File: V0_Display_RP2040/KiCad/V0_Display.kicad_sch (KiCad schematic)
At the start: 46 parts, among them J2 I2C Header 1, J3 SWD, J4 USB-TYPE-C-018, J7 USB_Header, J8 Conn_01x02, SW1 RESET, SW5 BOOTSEL, SW6 Killswitch, SW7 Rotary_Encoder_Switch, U1 AP2127K-3.3, U2 USBLC6-2P6, U3 74LVC1G17, U4 W25Q16JVUXIQ_TR, U5 RP2040, Y1 12Mhz

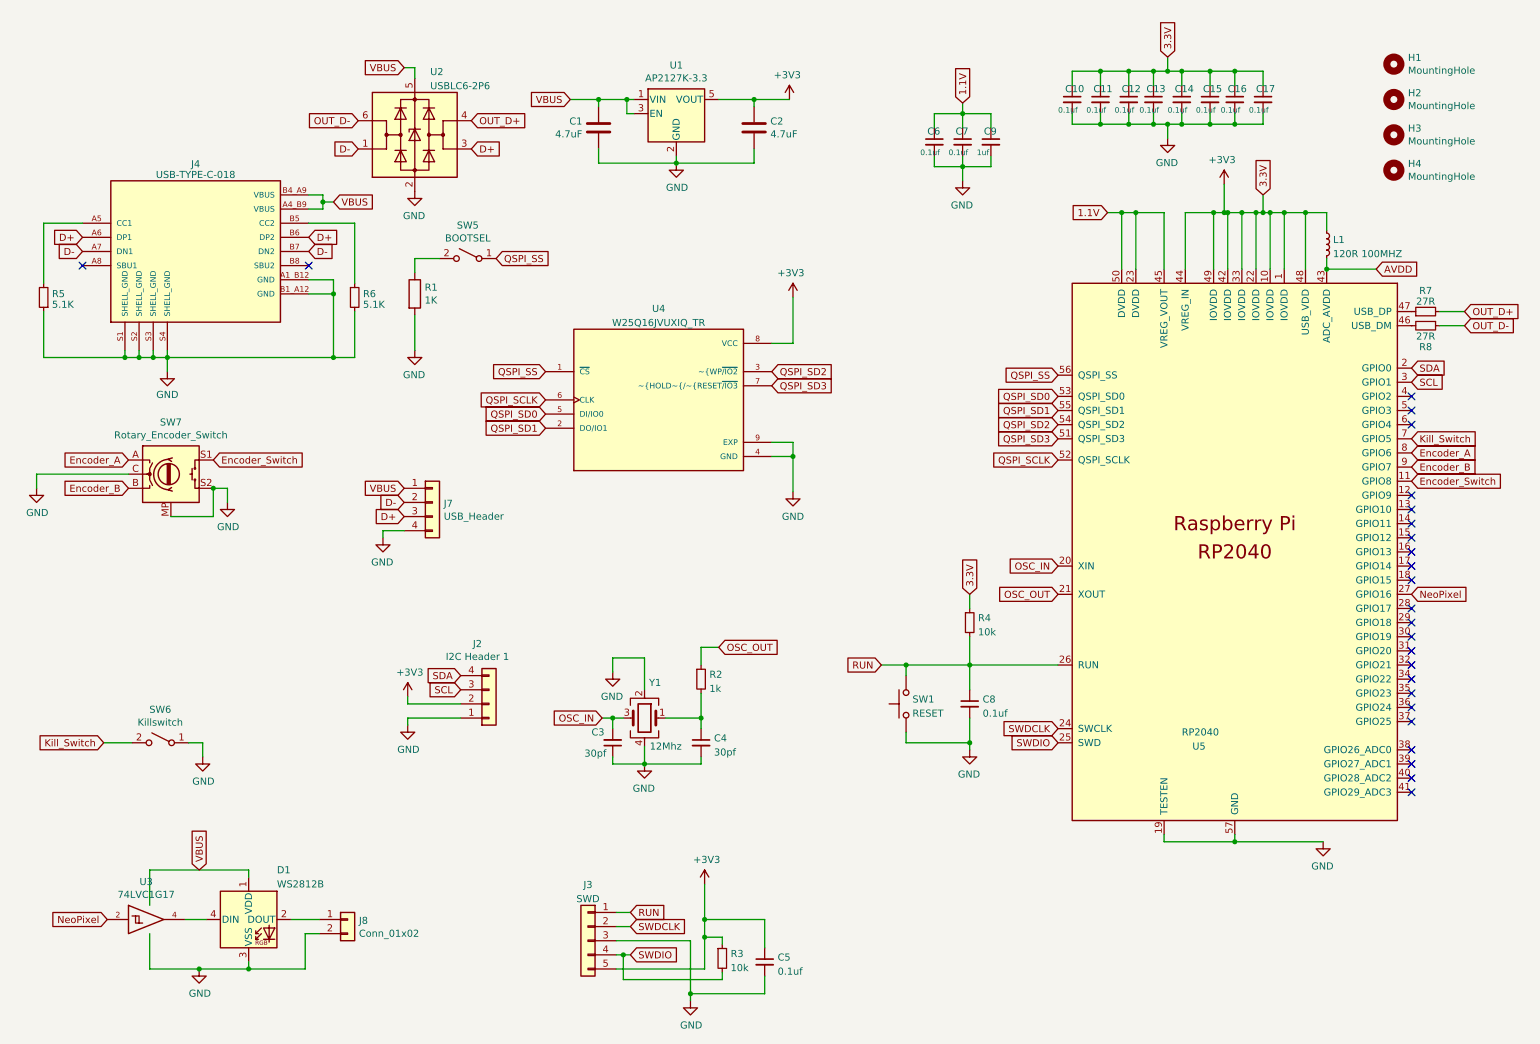
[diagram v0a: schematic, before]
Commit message: Several updates
Update to 2 layer board
vertical USB connector
updated fonts
Regenerated gerbers, BOM, and placement file
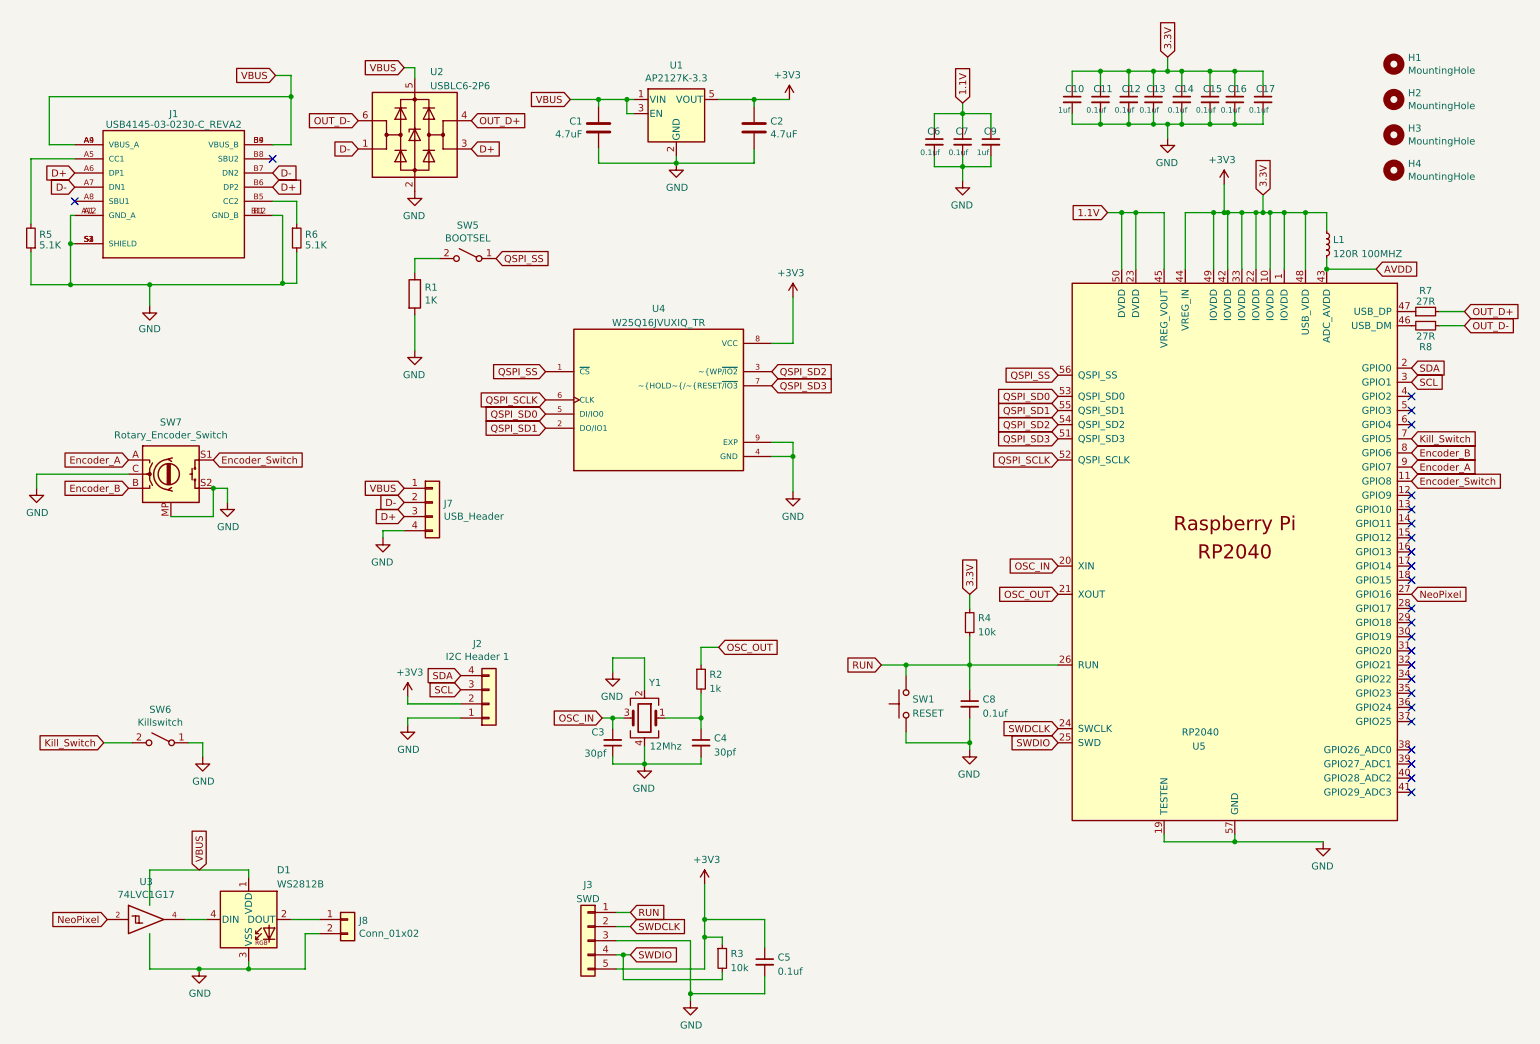
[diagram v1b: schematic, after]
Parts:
- removed J4: USB-TYPE-C-018, Voron0 2040 display:GCT_USB4105-GF-A, symbol Voron0 2040 library:USB4105-GF-A
- added J1: USB4145-03-0230-C_REVA2, USB4145-03-0230-C_REVA2:GCT_USB4145-03-0230-C_REVA2, symbol USB4145-03-0230-C_REVA2:USB4145-03-0230-C_REVA2
- C1, C2: symbol Voron0 2040 library:C -> Voron0 2040 display:C
- C10: value 0.1uf -> 1uf; symbol Voron0 2040 library:C_Small -> Voron0 2040 display:C_Small; LCSC C129131 -> C106254
- C11, C12, C13, C14, C15, C16, C17, C3, C4, C5, C6, C7, C8, C9: symbol Voron0 2040 library:C_Small -> Voron0 2040 display:C_Small
- D1: symbol Voron0 2040 library:WS2812B -> Voron0 2040 display:WS2812B
- H1, H2, H3, H4: symbol Voron0 2040 library:MountingHole -> Voron0 2040 display:MountingHole
- J2, J7: symbol Voron0 2040 library:Conn_01x04 -> Voron0 2040 display:Conn_01x04
- J3: symbol Voron0 2040 library:Conn_01x05 -> Voron0 2040 display:Conn_01x05
- J8: symbol Voron0 2040 library:Conn_01x02 -> Voron0 2040 display:Conn_01x02
- L1: symbol Voron0 2040 library:L_Small -> Voron0 2040 display:L_Small
- R1: symbol Voron0 2040 library:R -> Voron0 2040 display:R
- R2, R3, R4, R5, R6: symbol Voron0 2040 library:R_Small -> Voron0 2040 display:R_Small
- R7, R8: symbol Voron0 2040 library:R_Small -> Device:R_Small
- SW1: symbol Voron0 2040 library:SW_Push -> Voron0 2040 display:SW_Push
- SW5, SW6: symbol Voron0 2040 library:SW_SPST -> Voron0 2040 display:SW_SPST
- SW7: symbol Voron0 2040 library:Rotary_Encoder_Switch -> Voron0 2040 display:Rotary_Encoder_Switch
- U1: symbol Voron0 2040 library:AP2127K-3.3 -> Voron0 2040 display:AP2127K-3.3
- U2: symbol Voron0 2040 library:USBLC6-2P6 -> Voron0 2040 display:USBLC6-2P6
- U3: symbol Voron0 2040 library:74LVC1G17 -> Voron0 2040 display:74LVC1G17
- U4: symbol Voron0 2040 library:W25Q16JVUXIQ_TR -> Voron0 2040 display:W25Q16JVUXIQ_TR
- U5: symbol Voron0 2040 library:RP2040 -> Voron0 2040 display:RP2040
- Y1: symbol Voron0 2040 library:Crystal_GND24 -> Voron0 2040 display:Crystal_GND24
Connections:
- net D+: now also J1.A6 (DP1), J1.B6 (DP2)
- net D-: now also J1.A7 (DN1), J1.B7 (DN2)
- net Encoder_A: now also U5.9 (GPIO7); no longer U5.8 (GPIO6)
- net Encoder_B: now also U5.8 (GPIO6); no longer U5.9 (GPIO7)
- net GND: now also J1.A1 (GND_A), J1.A12 (GND_A), J1.B1 (GND_B), J1.B12 (GND_B), J1.S1 (SHIELD), J1.S2 (SHIELD), J1.S3 (SHIELD), J1.S4 (SHIELD)
- net VCC: now also J1.A4 (VBUS_A), J1.A9 (VBUS_A), J1.B4 (VBUS_B), J1.B9 (VBUS_B)
- net at R5.2: now also J1.A5 (CC1)
- net at R6.1: now also J1.B5 (CC2)
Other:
- moved on the sheet: R5, R6

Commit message: Update #2
Changed to SMD push buttons
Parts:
- SW1, SW5, SW6: footprint Voron0 2040 display:SW_PUSH_6mm -> Library:SW_Push_1P1T_NO_4.5x4.5mm; LCSC (none) -> C843607; MPN MJTP1230 -> (none); now in the parts list
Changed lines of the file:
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@@
   )
   (symbol (lib_id "Voron0 2040 display:SW_SPST") (at 95.25 55.245 0) (mirror y) (unit 1)
-    (in_bom no) (on_board yes) (dnp no)
+    (in_bom yes) (on_board yes) (dnp no)
     (property "Reference" "SW5" (at 95.25 49.276 0)
       (effects (font (size 1.27 1.27)))
@@
       (effects (font (size 1.27 1.27)))
     )
-    (property "Footprint" "Voron0 2040 display:SW_PUSH_6mm" (at 95.25 55.245 0)
+    (property "Footprint" "Library:SW_Push_1P1T_NO_4.5x4.5mm" (at 95.25 55.245 0)
       (effects (font (size 1.27 1.27)) hide)
     )
@@
       (effects (font (size 1.27 1.27)) hide)
     )
-    (property "MPN" "MJTP1230" (at 95.25 55.245 0)
+    (property "LCSC" "C843607" (at 95.25 55.245 0)
       (effects (font (size 1.27 1.27)) hide)
     )
@@
   )
   (symbol (lib_id "Voron0 2040 display:SW_SPST") (at 40.005 142.24 0) (mirror y) (unit 1)
-    (in_bom no) (on_board yes) (dnp no)
+    (in_bom yes) (on_board yes) (dnp no)
     (property "Reference" "SW6" (at 40.005 136.271 0)
       (effects (font (size 1.27 1.27)))
@@
       (effects (font (size 1.27 1.27)))
     )
-    (property "Footprint" "Voron0 2040 display:SW_PUSH_6mm" (at 40.005 142.24 0)
+    (property "Footprint" "Library:SW_Push_1P1T_NO_4.5x4.5mm" (at 40.005 142.24 0)
       (effects (font (size 1.27 1.27)) hide)
     )
@@
       (effects (font (size 1.27 1.27)) hide)
     )
-    (property "MPN" "MJTP1230" (at 40.005 142.24 0)
+    (property "LCSC" "C843607" (at 40.005 142.24 0)
       (effects (font (size 1.27 1.27)) hide)
     )
@@
   )
   (symbol (lib_id "Voron0 2040 display:SW_Push") (at 173.99 135.255 90) (unit 1)
-    (in_bom no) (on_board yes) (dnp no) (fields_autoplaced)
+    (in_bom yes) (on_board yes) (dnp no) (fields_autoplaced)
     (property "Reference" "SW1" (at 175.133 134.4203 90)
       (effects (font (size 1.27 1.27)) (justify right))
@@
       (effects (font (size 1.27 1.27)) (justify right))
     )
-    (property "Footprint" "Voron0 2040 display:SW_PUSH_6mm" (at 168.91 135.255 0)
+    (property "Footprint" "Library:SW_Push_1P1T_NO_4.5x4.5mm" (at 168.91 135.255 0)
       (effects (font (size 1.27 1.27)) hide)
     )
@@
       (effects (font (size 1.27 1.27)) hide)
     )
-    (property "MPN" "MJTP1230" (at 173.99 135.255 90)
-      (effects (font (size 1.27 1.27)) hide)
-    )
+    (property "LCSC" "C843607" (at 173.99 135.255 90)
+      (effects (font (size 1.27 1.27)) hide)
+    )

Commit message: Usability updates to hardware
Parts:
- added H5: MountingHole, Library:VoronLogo_6pt5mm_silkScreen, symbol Library:MountingHole
- added J4: USB_B_Micro, Library:MolexVertical&Horizontal_MicroB, symbol Library:USB_B_Micro
- added J5: GPIO, Connector_PinHeader_2.54mm:PinHeader_1x03_P2.54mm_Vertical, symbol Library:Conn_01x03
- added R9: 10k, Voron0 2040 display:R_0603_1608Metric, symbol Library:R_Small
- C1, C2: symbol Voron0 2040 display:C -> Library:C
- C10, C11, C12, C13, C14, C15, C16, C17, C3, C4, C5, C6, C7, C8, C9: symbol Voron0 2040 display:C_Small -> Library:C_Small
- D1: symbol Voron0 2040 display:WS2812B -> Library:WS2812B
- H1, H2, H3, H4: symbol Voron0 2040 display:MountingHole -> Library:MountingHole
- J1: symbol USB4145-03-0230-C_REVA2:USB4145-03-0230-C_REVA2 -> Library:USB4145-03-0230-C_REVA2; now not fitted
- J2: footprint Voron0 2040 display:1pt3in_OLED -> Library:1pt3in_OLED; symbol Voron0 2040 display:Conn_01x04 -> Library:Conn_01x04
- J3: symbol Voron0 2040 display:Conn_01x05 -> Library:Conn_01x05
- J7: symbol Voron0 2040 display:Conn_01x04 -> Library:Conn_01x04
- J8: symbol Voron0 2040 display:Conn_01x02 -> Library:Conn_01x02
- L1: symbol Voron0 2040 display:L_Small -> Library:L_Small
- R1: symbol Voron0 2040 display:R -> Library:R
- R2, R3, R4: symbol Voron0 2040 display:R_Small -> Library:R_Small
- R5, R6: symbol Voron0 2040 display:R_Small -> Library:R_Small; now not fitted
- R7, R8: symbol Device:R_Small -> Library:R_Small
- SW1: symbol Voron0 2040 display:SW_Push -> Library:SW_Push
- SW5, SW6: symbol Voron0 2040 display:SW_SPST -> Library:SW_SPST
- SW7: symbol Voron0 2040 display:Rotary_Encoder_Switch -> Library:Rotary_Encoder_Switch
- U1: symbol Voron0 2040 display:AP2127K-3.3 -> Library:AP2127K-3.3
- U2: symbol Voron0 2040 display:USBLC6-2P6 -> Library:USBLC6-2P6
- U3: symbol Voron0 2040 display:74LVC1G17 -> Library:74LVC1G17
- U4: symbol Voron0 2040 display:W25Q16JVUXIQ_TR -> Library:W25Q16JVUXIQ_TR
- U5: symbol Voron0 2040 display:RP2040 -> Library:RP2040
- Y1: symbol Voron0 2040 display:Crystal_GND24 -> Library:Crystal_GND24
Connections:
- net +3V3: now also R9.1
- net D+: now also J4.3 (D+)
- net D-: now also J4.2 (D-)
- net GND: now also SW5.2 (B), J4.4 (ID), J4.5 (GND), J4.6 (Shield); no longer R1.2
- net QSPI_SS: now also R1.2, R9.2; no longer SW5.1 (A)
- net VCC: now also J4.1 (VBUS)
- net at R1.1: now also SW5.1 (A); no longer SW5.2 (B)
- net GPIO20: now reaches U5.31 (GPIO20)
- net GPIO20: now also J5.1 (Pin_1)
- net GPIO21: now reaches U5.32 (GPIO21)
- net GPIO21: now also J5.2 (Pin_2)
- net GPIO22: now reaches U5.34 (GPIO22)
- net GPIO22: now also J5.3 (Pin_3)
- no-connect marks 25 -> 22
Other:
- moved on the sheet: R1, SW5, SW7

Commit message: Clean up
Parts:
- C1, C2: footprint Voron0 2040 display:C_0603_1608Metric -> Library:C_0603_1608Metric; LCSC C326580 -> C19666
- C10, C9: footprint Voron0 2040 display:C_0402_1005Metric -> Library:C_0402_1005Metric; LCSC C106254 -> C52923
- C11, C12, C13, C14, C15, C16, C17, C5, C6, C7, C8: footprint Voron0 2040 display:C_0402_1005Metric -> Library:C_0402_1005Metric; LCSC C129131 -> C1525
- C3, C4: footprint Voron0 2040 display:C_0402_1005Metric -> Library:C_0402_1005Metric
- D1: footprint Voron0 2040 display:LED_WS2812B_PLCC4_5.0x5.0mm_P3.2mm -> Library:LED_WS2812B_PLCC4_5.0x5.0mm_P3.2mm; LCSC C114586 -> C2761795
- H1, H2, H3, H4: footprint Voron0 2040 display:MountingHole_3.2mm_M3 -> Library:MountingHole_3.2mm_M3
- J1: footprint USB4145-03-0230-C_REVA2:GCT_USB4145-03-0230-C_REVA2 -> Library:GCT_USB4145-03-0230-C_REVA2; Availability In Stock -> (none); Check_prices https://www.snapeda.com/parts/USB4145-03-0230-C/Global+Conn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 -> (none); MANUFACTURER GCT -> (none); MAXIMUM_PACKAGE_HEIGHT 7.66mm -> (none); MF Global Connector Technology -> (none); MP USB4145-03-0230-C -> (none); MPN (none) -> USB4145-03-0230-C; PARTREV A2 -> (none); Package None -> (none); Price None -> (none); SNAPEDA_PN USB4145-03-0230-C -> (none); STANDARD Manufacturer Recommendations -> (none); SnapEDA_Link https://www.snapeda.com/parts/USB4145-03-0230-C/Global+Conn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 -> (none)
- J3: footprint Voron0 2040 display:PinHeader_1x05_P2.54mm_Vertical -> Library:PinHeader_1x05_P2.54mm_Vertical
- J7: footprint Voron0 2040 display:PinHeader_1x04_P2.54mm_Vertical -> Library:PinHeader_1x04_P2.54mm_Vertical
- J8: footprint Voron0 2040 display:PinHeader_1x02_P2.54mm_Vertical -> Library:PinHeader_1x02_P2.54mm_Vertical
- L1: footprint Voron0 2040 display:L_0402_1005Metric -> Library:L_0402_1005Metric
- R1: footprint Voron0 2040 display:R_0603_1608Metric -> Library:R_0603_1608Metric; LCSC C4295595 -> C21190
- R2: footprint Voron0 2040 display:R_0402_1005Metric -> Library:R_0603_1608Metric; LCSC C852624 -> C21190
- R3, R4, R9: footprint Voron0 2040 display:R_0603_1608Metric -> Library:R_0603_1608Metric; LCSC C2139679 -> C25804
- R5, R6: footprint Voron0 2040 display:R_0402_1005Metric -> Library:R_0603_1608Metric; LCSC C105873 -> C23186
- R7, R8: footprint Voron0 2040 display:R_0402_1005Metric -> Library:R_0402_1005Metric
- SW7: footprint Voron0 2040 display:EN11_Encoder -> Library:EN11_Encoder
- U1: footprint Voron0 2040 display:SOT-23-5 -> Library:SOT-23-5
- U2: footprint Voron0 2040 display:SOT-666 -> Library:SOT-666
- U3: footprint Voron0 2040 display:SOT-753 -> Library:SOT-753
- U4: footprint Voron0 2040 display:IC_W25Q16JVUXIQ_TR -> Library:IC_W25Q16JVUXIQ_TR
- U5: footprint Voron0 2040 display:RP2040-QFN-56 -> Library:RP2040-QFN-56
- Y1: footprint Voron0 2040 display:Crystal_SMD_3225-4Pin_3.2x2.5mm -> Library:Crystal_SMD_3225-4Pin_3.2x2.5mm

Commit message: Fixed up gerbers
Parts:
- H5, J1, R5, R6: now left out of the parts list
- J4: LCSC (none) -> C136000
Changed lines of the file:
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@@
+      (effects (font (size 1.27 1.27)) hide)
+    )
+    (property "LCSC" "C136000" (at 27.686 85.852 0)
       (effects (font (size 1.27 1.27)) hide)
     )
@@
   )
   (symbol (lib_id "Library:MountingHole") (at 265.938 160.02 0) (unit 1)
-    (in_bom yes) (on_board yes) (dnp no) (fields_autoplaced)
+    (in_bom no) (on_board yes) (dnp no) (fields_autoplaced)
     (property "Reference" "H5" (at 268.478 158.8079 0)
       (effects (font (size 1.27 1.27)) (justify left))
@@
     )
     (property "Datasheet" "~" (at 265.938 160.02 0)
+      (effects (font (size 1.27 1.27)) hide)
+    )
+    (property "Sim.Enable" "0" (at 265.938 160.02 0)
       (effects (font (size 1.27 1.27)) hide)
     )
@@
   )
   (symbol (lib_id "Library:USB4145-03-0230-C_REVA2") (at 42.418 42.418 0) (unit 1)
-    (in_bom yes) (on_board no) (dnp yes) (fields_autoplaced)
+    (in_bom no) (on_board no) (dnp yes) (fields_autoplaced)
     (property "Reference" "J1" (at 42.418 29.2481 0)
       (effects (font (size 1.27 1.27)))
@@
   )
   (symbol (lib_id "Library:R_Small") (at 64.516 51.562 0) (unit 1)
-    (in_bom yes) (on_board no) (dnp yes) (fields_autoplaced)
+    (in_bom no) (on_board no) (dnp yes) (fields_autoplaced)
     (property "Reference" "R6" (at 66.0146 50.9183 0)
       (effects (font (size 1.27 1.27)) (justify left))
@@
   )
   (symbol (lib_id "Library:R_Small") (at 16.764 51.562 180) (unit 1)
-    (in_bom yes) (on_board no) (dnp yes) (fields_autoplaced)
+    (in_bom no) (on_board no) (dnp yes) (fields_autoplaced)
     (property "Reference" "R5" (at 18.2626 50.9183 0)
       (effects (font (size 1.27 1.27)) (justify right))
